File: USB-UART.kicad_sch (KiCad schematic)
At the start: 41 parts, among them J1 USB_A, J2 Conn_01x06, J3 Conn_01x06, J4 Conn_01x06, U1 WE-TVS-82400152, U2 FT230XQ, U3 SN74LVC2T45DCUR, U4 SN74LVC2T45DCUR, U5 MAX232

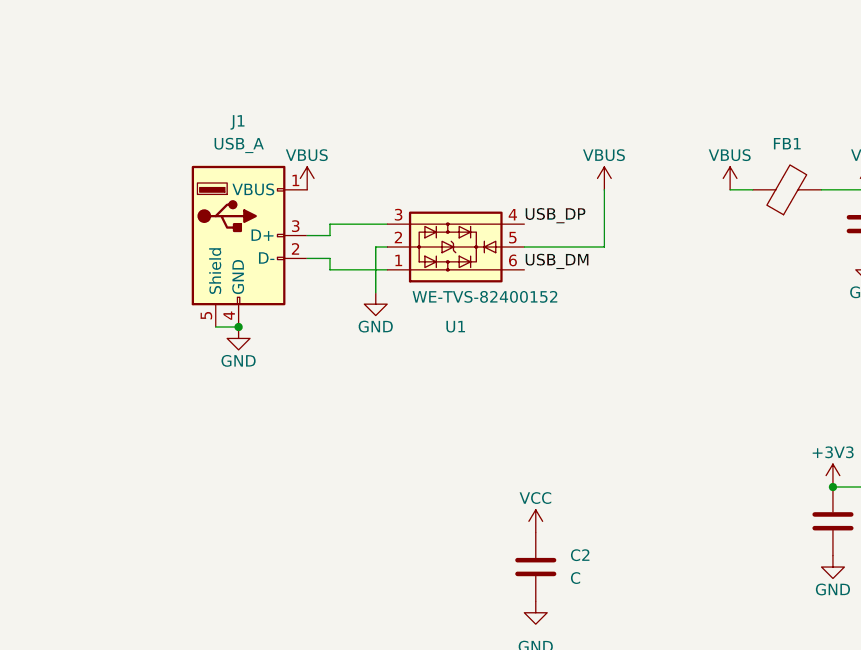
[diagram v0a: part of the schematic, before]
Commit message: change connector to USBC
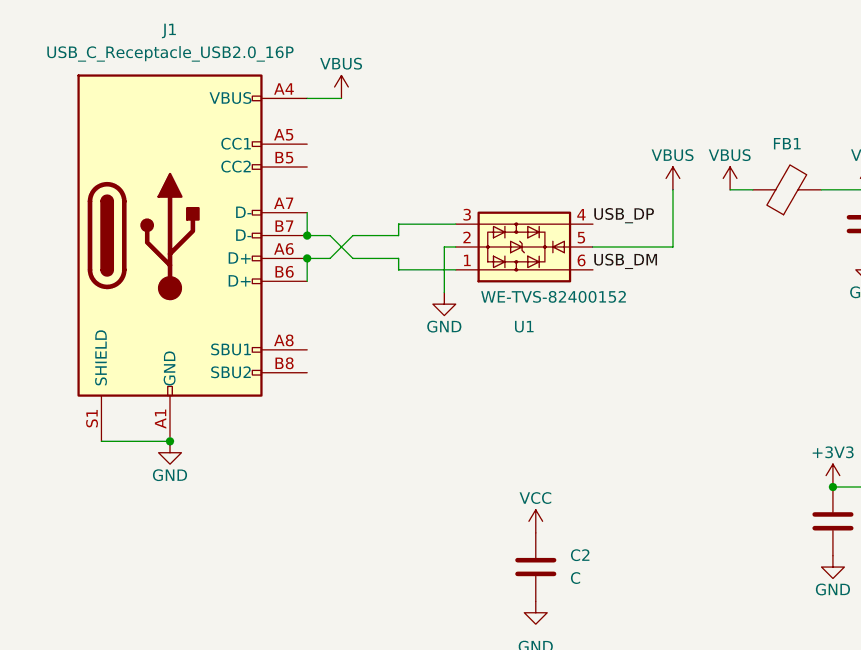
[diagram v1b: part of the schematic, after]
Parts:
- removed J1: USB_A, Connector_USB_gk:USB3_A_Molex_480371000_Plug, symbol Connector:USB_A
- added J1: USB_C_Receptacle_USB2.0_16P, all_gk_fp_Ki8:USB_C_Receptacle_Wuerth_629722000214, symbol Connector:USB_C_Receptacle_USB2.0_16P
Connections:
- net GND: now also J1.A1 (GND), J1.A12 (GND), J1.B1 (GND), J1.B12 (GND), J1.S1 (SHIELD)
- net VBUS: now also J1.A4 (VBUS), J1.A9 (VBUS), J1.B4 (VBUS), J1.B9 (VBUS)
- net at U1.1: now also J1.A7 (D-), J1.B7 (D-)
- net at U1.3: now also J1.A6 (D+), J1.B6 (D+)
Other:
- moved on the sheet: U1
